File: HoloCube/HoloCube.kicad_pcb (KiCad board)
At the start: 4 copper layers, 30 x 29 mm, 37 parts, among them J1 ESPProgUART_RX, J2 Conn_01x12_MountingPin, J3 USB_C_Receptacle_USB2.0, J4 Micro_SD_Card, Q1 MMBT3904, U1 ESP32-PICO-D4, U2 LIS2DH12TR, U3 BH1750FVI-TR, U4 XC6209

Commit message: 投板版本
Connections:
- U1 pad 10: /IO34 -> unconnected-(U1-Pad10)
- U1 pad 11: /IO35 -> unconnected-(U1-Pad11)
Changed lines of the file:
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@@
   (net 57 "/I2C_SDA")
   (net 58 "unconnected-(U1-Pad18)")
-  (net 59 "/IO34")
-  (net 60 "/IO35")
+  (net 59 "unconnected-(U1-Pad10)")
+  (net 60 "unconnected-(U1-Pad11)")
   (net 61 "/DC")
   (net 62 "/BTN_Right")
@@
       (net 2 "/EN") (pinfunction "EN") (pintype "input"))
     (pad "10" smd roundrect (at -3.45 1.75) (size 0.8 0.25) (layers "F.Cu" "F.Paste" "F.Mask") (roundrect_rratio 0.25)
-      (net 59 "/IO34") (pinfunction "IO34") (pintype "input"))
+      (net 59 "unconnected-(U1-Pad10)") (pinfunction "IO34") (pintype "input+no_connect"))
     (pad "11" smd roundrect (at -3.45 2.25) (size 0.8 0.25) (layers "F.Cu" "F.Paste" "F.Mask") (roundrect_rratio 0.25)
-      (net 60 "/IO35") (pinfunction "IO35") (pintype "input"))
+      (net 60 "unconnected-(U1-Pad11)") (pinfunction "IO35") (pintype "input+no_connect"))
     (pad "12" smd roundrect (at -3.45 2.75) (size 0.8 0.25) (layers "F.Cu" "F.Paste" "F.Mask") (roundrect_rratio 0.25)
       (net 57 "/I2C_SDA") (pinfunction "IO32") (pintype "bidirectional"))
@@
       (net 63 "/BTN_Left") (pinfunction "IO14") (pintype "bidirectional"))
     (pad "18" smd roundrect (at -0.25 3.45) (size 0.25 0.8) (layers "F.Cu" "F.Paste" "F.Mask") (roundrect_rratio 0.25)
-      (net 58 "unconnected-(U1-Pad18)") (pinfunction "IO12") (pintype "bidirectional"))
+      (net 58 "unconnected-(U1-Pad18)") (pinfunction "IO12") (pintype "bidirectional+no_connect"))
     (pad "19" smd roundrect (at 0.25 3.45) (size 0.25 0.8) (layers "F.Cu" "F.Paste" "F.Mask") (roundrect_rratio 0.25)
       (net 7 "+3V3") (pinfunction "VDD3P3_RTC") (pintype "power_in"))
@@
     (property "Sheetname" "")
     (attr through_hole)
-    (fp_text reference "U3" (at 1.226565 -1.937485 -90) (layer "F.SilkS") hide
+    (fp_text reference "U3" (at 1.226565 -1.937485 -90) (layer "F.SilkS")
       (effects (font (size 1.001283 1.001283) (thickness 0.15)))
     )
@@
       (effects (font (size 1.001039 1.001039) (thickness 0.15)))
     )
+    (fp_line (start -0.78 0.8) (end 0.78 0.8) (layer "F.SilkS") (width 0.127))
     (fp_line (start 0.78 -0.8) (end -0.78 -0.8) (layer "F.SilkS") (width 0.127))
-    (fp_line (start -0.78 0.8) (end 0.78 0.8) (layer "F.SilkS") (width 0.127))
     (fp_circle (center -2.1 -0.5) (end -2 -0.5) (layer "F.SilkS") (width 0.2) (fill none))
+    (fp_line (start 1.9 -1.05) (end 1.9 1.05) (layer "F.CrtYd") (width 0.05))
     (fp_line (start 1.9 1.05) (end -1.9 1.05) (layer "F.CrtYd") (width 0.05))
+    (fp_line (start -1.9 1.05) (end -1.9 -1.05) (layer "F.CrtYd") (width 0.05))
     (fp_line (start -1.9 -1.05) (end 1.9 -1.05) (layer "F.CrtYd") (width 0.05))
-    (fp_line (start -1.9 1.05) (end -1.9 -1.05) (layer "F.CrtYd") (width 0.05))
-    (fp_line (start 1.9 -1.05) (end 1.9 1.05) (layer "F.CrtYd") (width 0.05))
+    (fp_line (start 1.3 0.8) (end 1.3 -0.8) (layer "F.Fab") (width 0.127))
+    (fp_line (start 1.3 -0.8) (end -1.3 -0.8) (layer "F.Fab") (width 0.127))
     (fp_line (start -1.3 0.8) (end 1.3 0.8) (layer "F.Fab") (width 0.127))
-    (fp_line (start 1.3 0.8) (end 1.3 -0.8) (layer "F.Fab") (width 0.127))
     (fp_line (start -1.3 -0.8) (end -1.3 0.8) (layer "F.Fab") (width 0.127))
-    (fp_line (start 1.3 -0.8) (end -1.3 -0.8) (layer "F.Fab") (width 0.127))
     (fp_circle (center -2.1 -0.5) (end -2 -0.5) (layer "F.Fab") (width 0.2) (fill none))
     (pad "1" smd rect (at -1.375 -0.5 270) (size 0.55 0.25) (layers "F.Cu" "F.Paste" "F.Mask")
@@
     (property "Sheetname" "")
     (attr through_hole)
-    (fp_text reference "U2" (at 0.26154 -2.02186 180) (layer "F.SilkS") hide
+    (fp_text reference "U2" (at 0.26154 -2.02186 180) (layer "F.SilkS")
       (effects (font (size 0.810205 0.810205) (thickness 0.15)))
     )
@@
       (effects (font (size 0.810409 0.810409) (thickness 0.15)))
     )
+    (fp_line (start -1.08 -1.105) (end -0.61 -1.105) (layer "F.SilkS") (width 0.127))
+    (fp_line (start -0.61 1.105) (end -1.08 1.105) (layer "F.SilkS") (width 0.127))
+    (fp_line (start 1.08 1.105) (end 0.61 1.105) (layer "F.SilkS") (width 0.127))
     (fp_line (start 0.61 -1.105) (end 1.08 -1.105) (layer "F.SilkS") (width 0.127))
-    (fp_line (start -1.08 -1.105) (end -0.61 -1.105) (layer "F.SilkS") (width 0.127))
-    (fp_line (start 1.08 1.105) (end 0.61 1.105) (layer "F.SilkS") (width 0.127))
-    (fp_line (start -0.61 1.105) (end -1.08 1.105) (layer "F.SilkS") (width 0.127))
     (fp_circle (center -1.35 -0.8) (end -1.3 -0.8) (layer "F.SilkS") (width 0.1) (fill none))
     (fp_line (start -1.24 -1.24) (end 1.24 -1.24) (layer "F.CrtYd") (width 0.05))
     (fp_line (start -1.24 1.24) (end -1.24 -1.24) (layer "F.CrtYd") (width 0.05))
+    (fp_line (start 1.24 -1.24) (end 1.24 1.24) (layer "F.CrtYd") (width 0.05))
     (fp_line (start 1.24 1.24) (end -1.24 1.24) (layer "F.CrtYd") (width 0.05))
-    (fp_line (start 1.24 -1.24) (end 1.24 1.24) (layer "F.CrtYd") (width 0.05))
     (fp_line (start -1.08 -1.08) (end 1.08 -1.08) (layer "F.Fab") (width 0.127))
+    (fp_line (start -1.08 1.08) (end -1.08 -1.08) (layer "F.Fab") (width 0.127))
     (fp_line (start 1.08 1.08) (end -1.08 1.08) (layer "F.Fab") (width 0.127))
-    (fp_line (start -1.08 1.08) (end -1.08 -1.08) (layer "F.Fab") (width 0.127))
     (fp_line (start 1.08 -1.08) (end 1.08 1.08) (layer "F.Fab") (width 0.127))
     (fp_circle (center -0.78 -0.8) (end -0.73 -0.8) (layer "F.Fab") (width 0.1) (fill none))

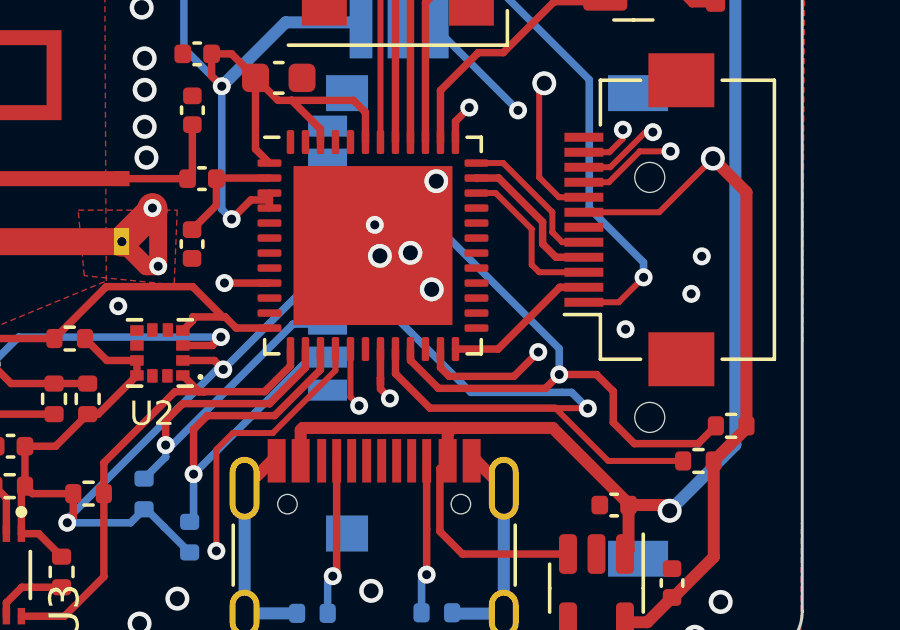
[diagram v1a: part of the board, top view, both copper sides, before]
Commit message: Fix most 3D parts
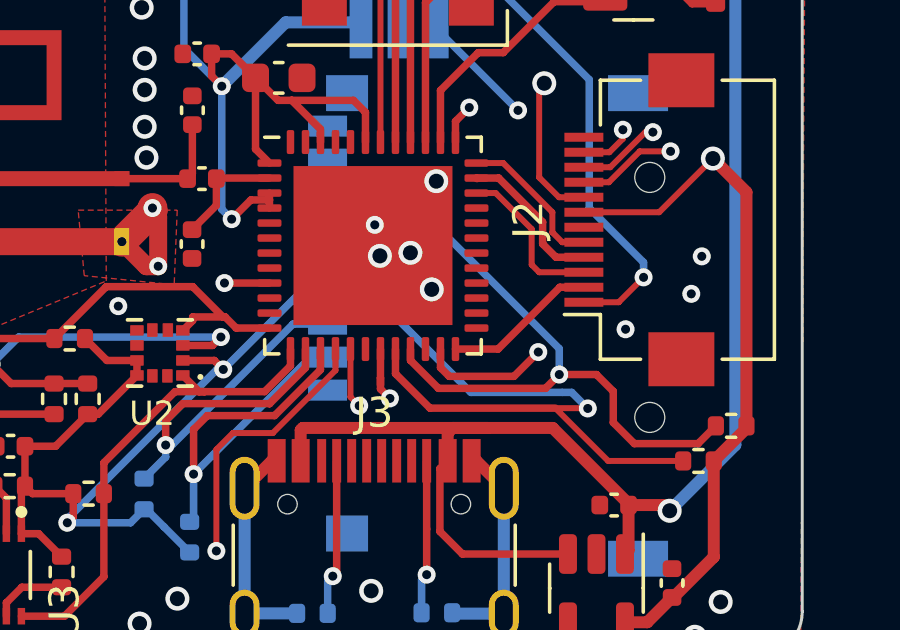
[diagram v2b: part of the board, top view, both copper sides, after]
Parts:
- J2: footprint Connector_FFC-FPC:Hirose_FH12-12S-0.5SH_1x12-1MP_P0.50mm_Horizontal -> KisonNew:Hirose_FH12-12S-0.5SH_1x12-1MP_P0.50mm_Horizontal
- J3: footprint Connector_USB:USB_C_Receptacle_HRO_TYPE-C-31-M-12 -> KisonNew:USB_C_Receptacle_HRO_TYPE-C-31-M-12
